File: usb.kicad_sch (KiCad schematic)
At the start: 49 parts, among them Q1 PJE138K, Q4 PJE138K, U1 MPFS250T-FCVG484, U13 USB3315-CP-TR, U22 PI3USB102GZLEX, U23 PI3USB102GZLEX, U28 USB2422-I/MJ, Y1 Oscillator_24MHz_ESC_2016MV

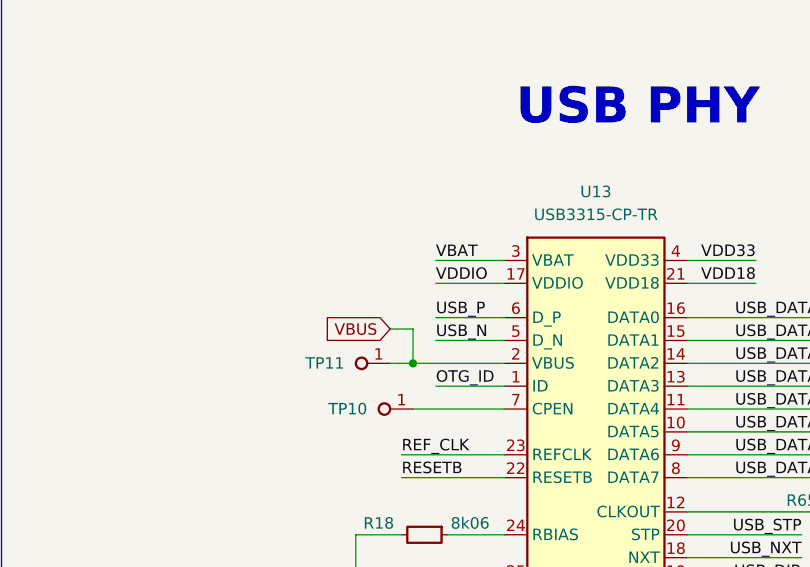
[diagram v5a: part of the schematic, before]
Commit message: [#56952] Place top designators, clean ERC
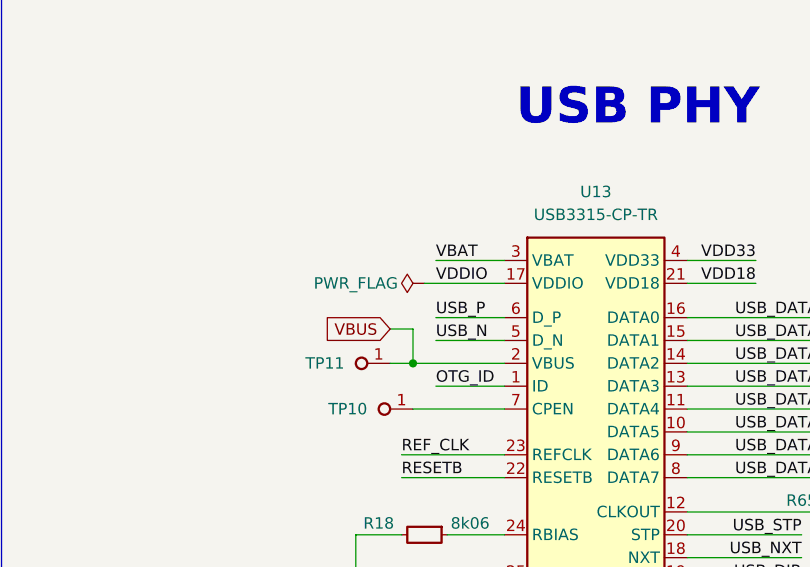
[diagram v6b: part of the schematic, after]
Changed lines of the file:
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@@
     (stroke (width 0) (type default))
   )
-  (wire (pts (xy 194.31 130.81) (xy 201.93 130.81))
-    (stroke (width 0) (type default))
-  )
   (wire (pts (xy 105.41 161.29) (xy 105.41 165.1))
     (stroke (width 0) (type default))
@@
     (stroke (width 0) (type default))
   )
+  (wire (pts (xy 193.04 130.81) (xy 201.93 130.81))
+    (stroke (width 0) (type default))
+  )
   (wire (pts (xy 158.75 198.12) (xy 165.1 198.12))
     (stroke (width 0) (type default))
@@
         )
       )
+    )
+  )
+  (symbol (lib_id "antmicropower:PWR_FLAG") (at 193.04 130.81 90) (unit 1)
+    (in_bom yes) (on_board yes) (dnp no)
+    (property "Reference" "#FLG07" (at 191.135 130.81 0)
+      (effects (font (size 1.27 1.27)) hide)
+    )
+    (property "Value" "PWR_FLAG" (at 185.42 130.81 90)
+      (effects (font (size 1.27 1.27)))
+    )
+    (property "Footprint" "" (at 193.04 130.81 0)
+      (effects (font (size 1.27 1.27)) hide)
+    )
+    (property "Datasheet" "" (at 193.04 130.81 0)
+      (effects (font (size 1.27 1.27)) hide)
+    )
+    (pin "1")
+    (instances
+      (project "polarfire-som"
+        (path "/db4a0d3e-2eb3-499e-977d-6eb378cfd3ed/d93d65d4-e21e-44e3-82fb-4ad52468a6b3"
+          (reference "#FLG07") (unit 1)
+        )
+      )

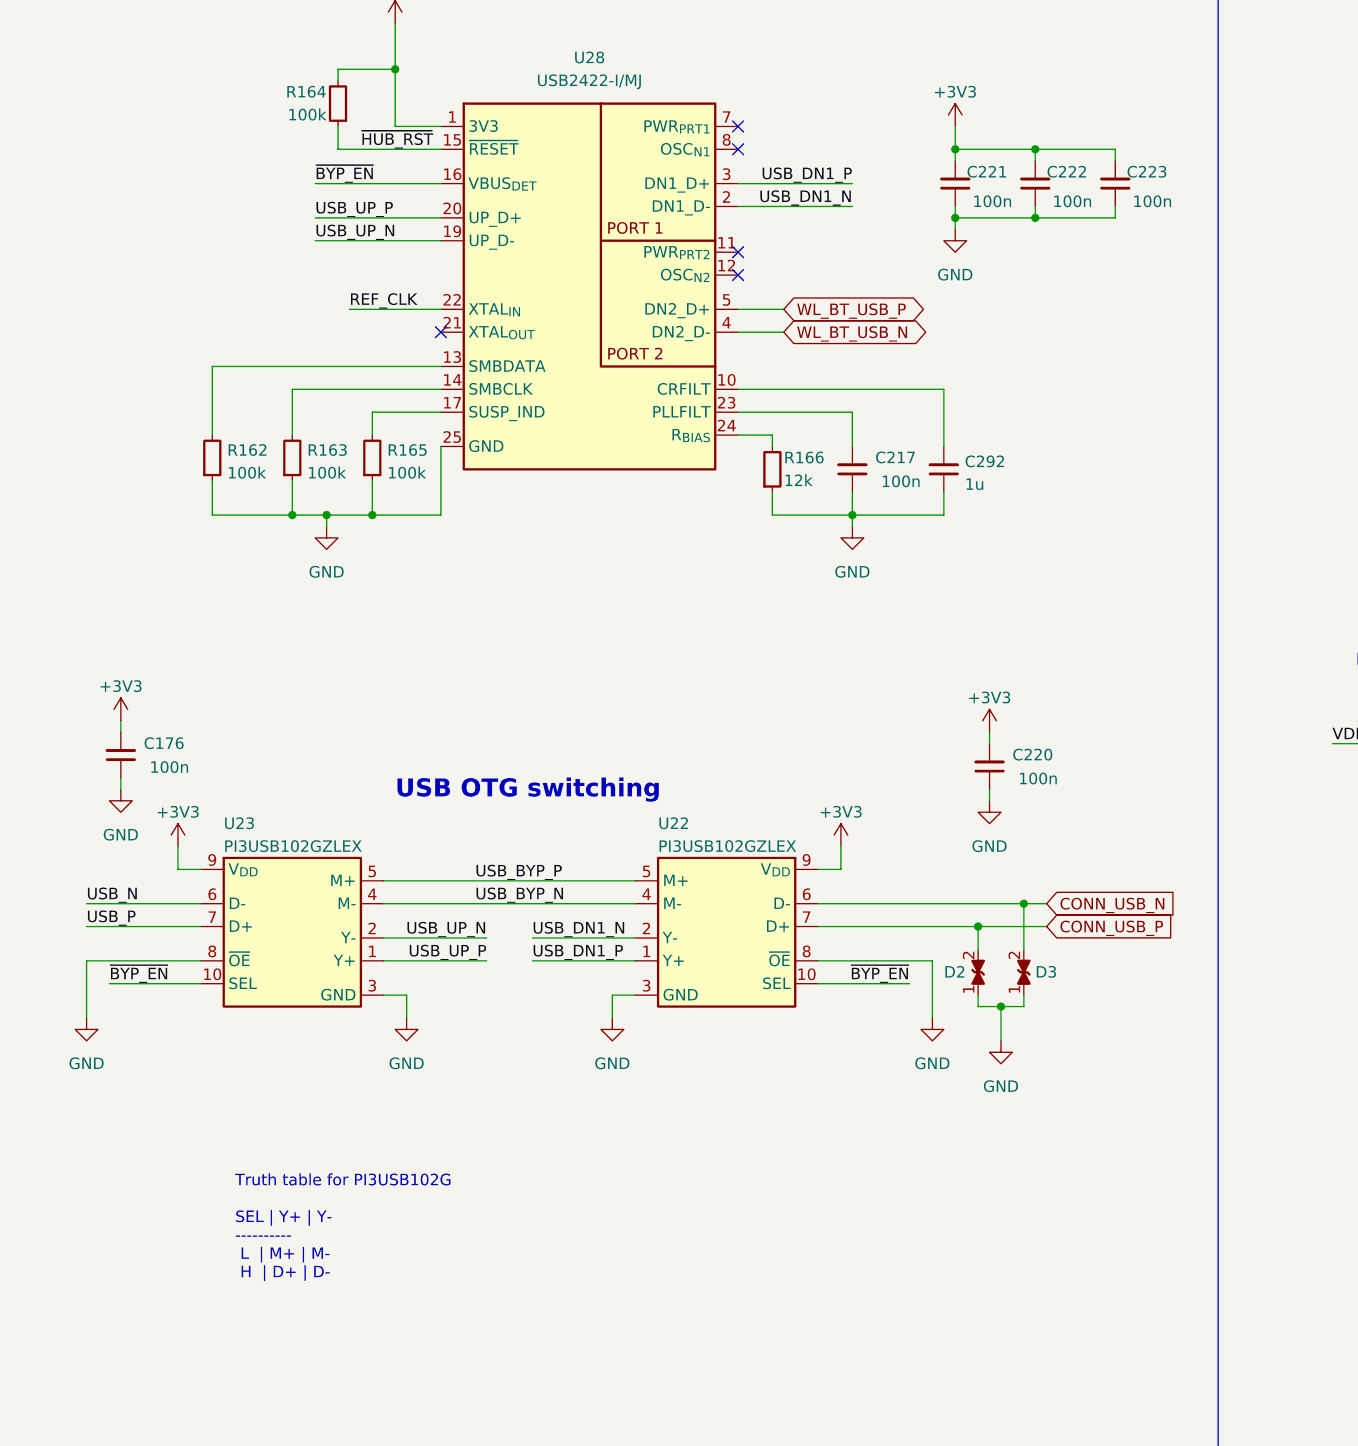
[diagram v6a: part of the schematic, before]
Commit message: [#57422] Add 0R resistors on SENSE+ lines, swap USB lines
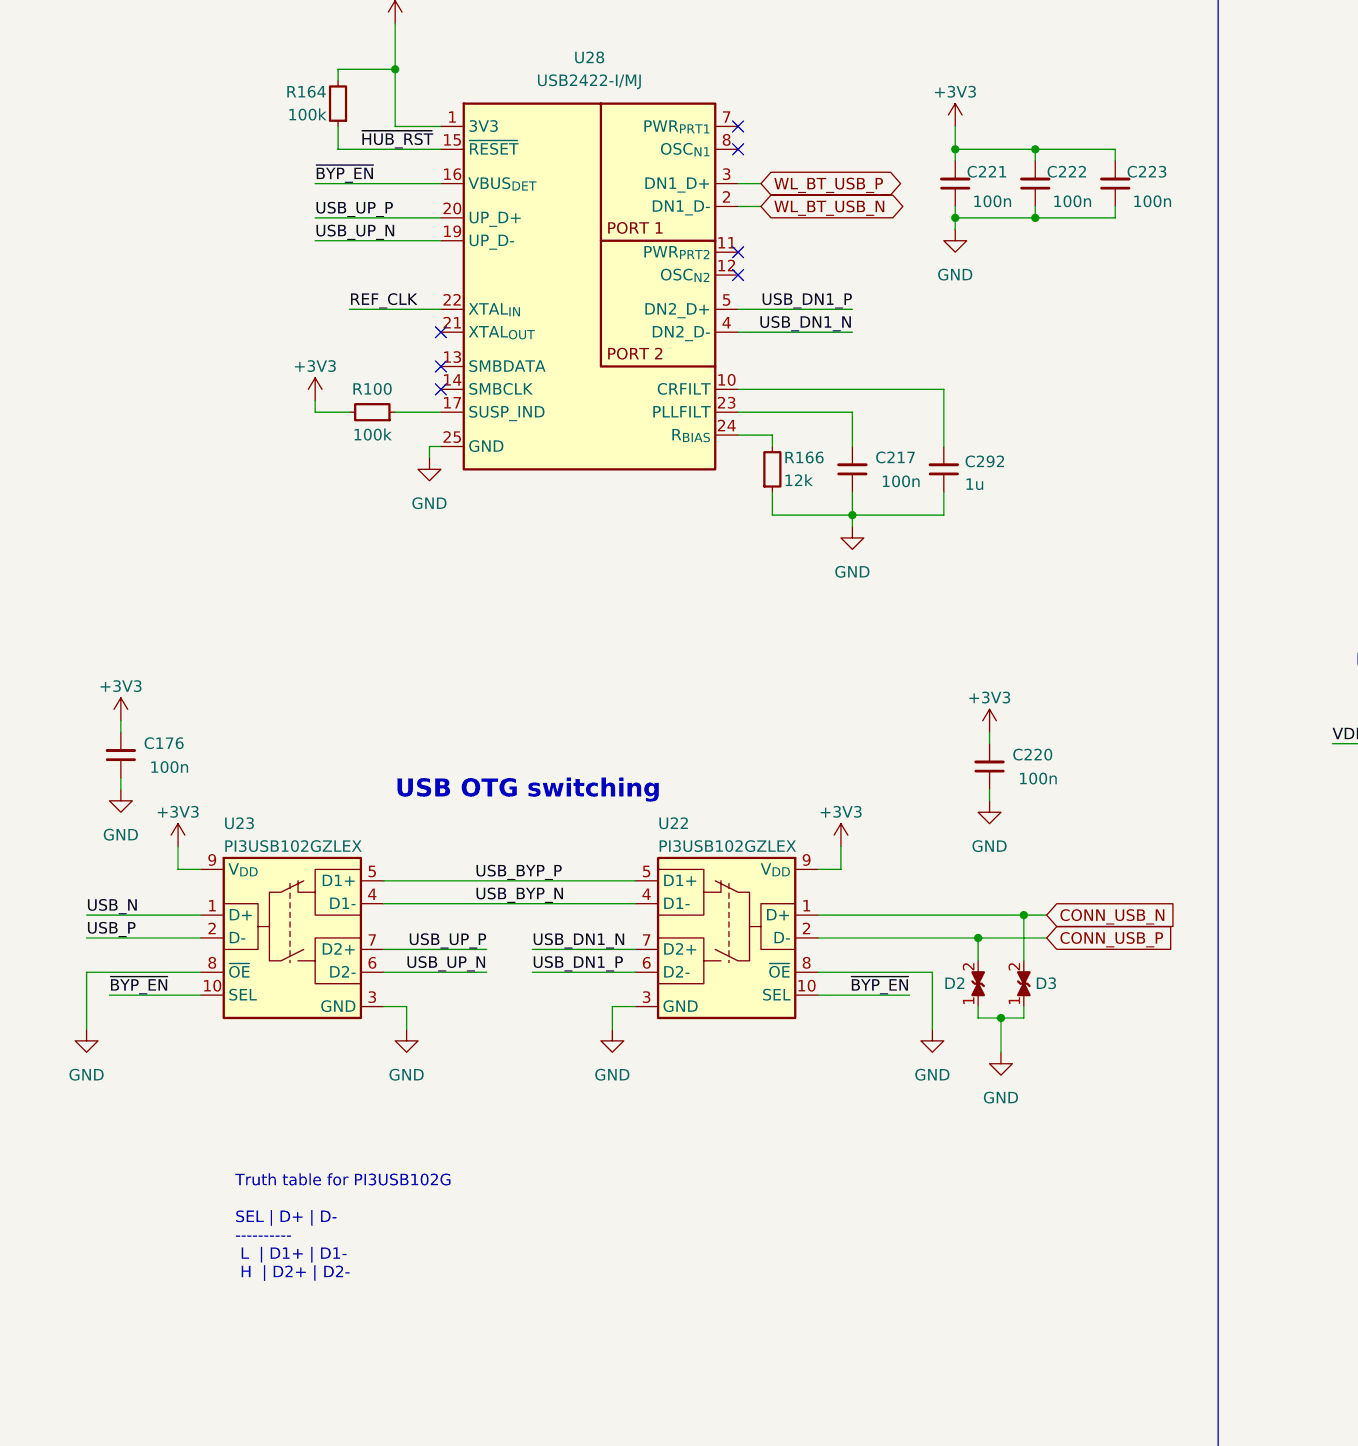
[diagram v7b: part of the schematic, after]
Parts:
- removed R162, R163, R165: R_100k_0402, antmicro-footprints:R_0402_1005Metric, symbol antmicroResistors0402:R_100k_0402
- added R100: R_100k_0402, antmicro-footprints:R_0402_1005Metric, symbol antmicroResistors0402:R_100k_0402
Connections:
- net +3V3: now also R100.2
- net CONN_USB_N: now also U22.1 (D+); no longer U22.6 (D-)
- net CONN_USB_P: now also U22.2 (D-); no longer U22.7 (D+)
- net USB_DN1_N: now also U22.7 (D2+), U28.4 (DN2_D-); no longer U22.2 (Y-), U28.2 (DN1_D-)
- net USB_DN1_P: now also U22.6 (D2-), U28.5 (DN2_D+); no longer U22.1 (Y+), U28.3 (DN1_D+)
- net USB_N: now also U23.1 (D+); no longer U23.6 (D-)
- net USB_P: now also U23.2 (D-); no longer U23.7 (D+)
- net USB_UP_N: now also U23.6 (D2-); no longer U23.2 (Y-)
- net USB_UP_P: now also U23.7 (D2+); no longer U23.1 (Y+)
- net WL_BT_USB_N: now also U28.2 (DN1_D-); no longer U28.4 (DN2_D-)
- net WL_BT_USB_P: now also U28.3 (DN1_D+); no longer U28.5 (DN2_D+)
- net at U28.17 (SUSP_IND): now also R100.1
- no-connect marks 11 -> 13
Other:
- note added: "Truth table for PI3USB102G SEL | D+ | D- ---------- L | D1+ | D1- H | D2+ | D2-"
- note removed: "Truth table for PI3USB102G SEL | Y+ | Y- ---------- L | M+ | M- H | D+ | D-"
- moved on the sheet: D2, D3

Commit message: [#57422] Update DNP
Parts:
- R58: now not fitted
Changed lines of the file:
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@@
   )
   (symbol (lib_id "antmicroResistors0402:R_10k_0402") (at 266.7 121.92 90) (unit 1)
-    (in_bom yes) (on_board yes) (dnp no)
+    (in_bom yes) (on_board yes) (dnp yes)
     (property "Reference" "R58" (at 268.605 118.1099 90)
       (effects (font (size 1.27 1.27) (thickness 0.15)) (justify right))
@@
     )
     (property "DNP" "DNP" (at 266.7 119.38 0)
-      (effects (font (size 1.27 1.27)))
+      (effects (font (size 1.27 1.27)) hide)
     )
     (pin "1")
